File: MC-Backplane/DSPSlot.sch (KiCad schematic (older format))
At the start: 0 parts

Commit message: added reverse polarity protection circuit and fuse
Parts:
- added J?: DB37_Female, symbol Connector:DB37_Female
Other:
- note added: "placeholder connector"
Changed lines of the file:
@@
 $Descr A4 11693 8268
 encoding utf-8
-Sheet 1 5
+Sheet 5 5
 Title ""
 Date ""
@@
 Comment4 ""
 $EndDescr
+$Comp
+L Connector:DB37_Female J?
+U 1 1 61EE6699
+P 9050 3750
+F 0 "J?" H 9230 3784 50  0000 L CNN
+F 1 "DB37_Female" H 9230 3693 50  0000 L CNN
+F 2 "" H 9050 3750 50  0001 C CNN
+F 3 " ~" H 9050 3750 50  0001 C CNN
+	1    9050 3750
+	1    0    0    -1
+$EndComp
+Text Notes 9400 1550 0    50   ~ 0
+placeholder connector
 $EndSCHEMATC

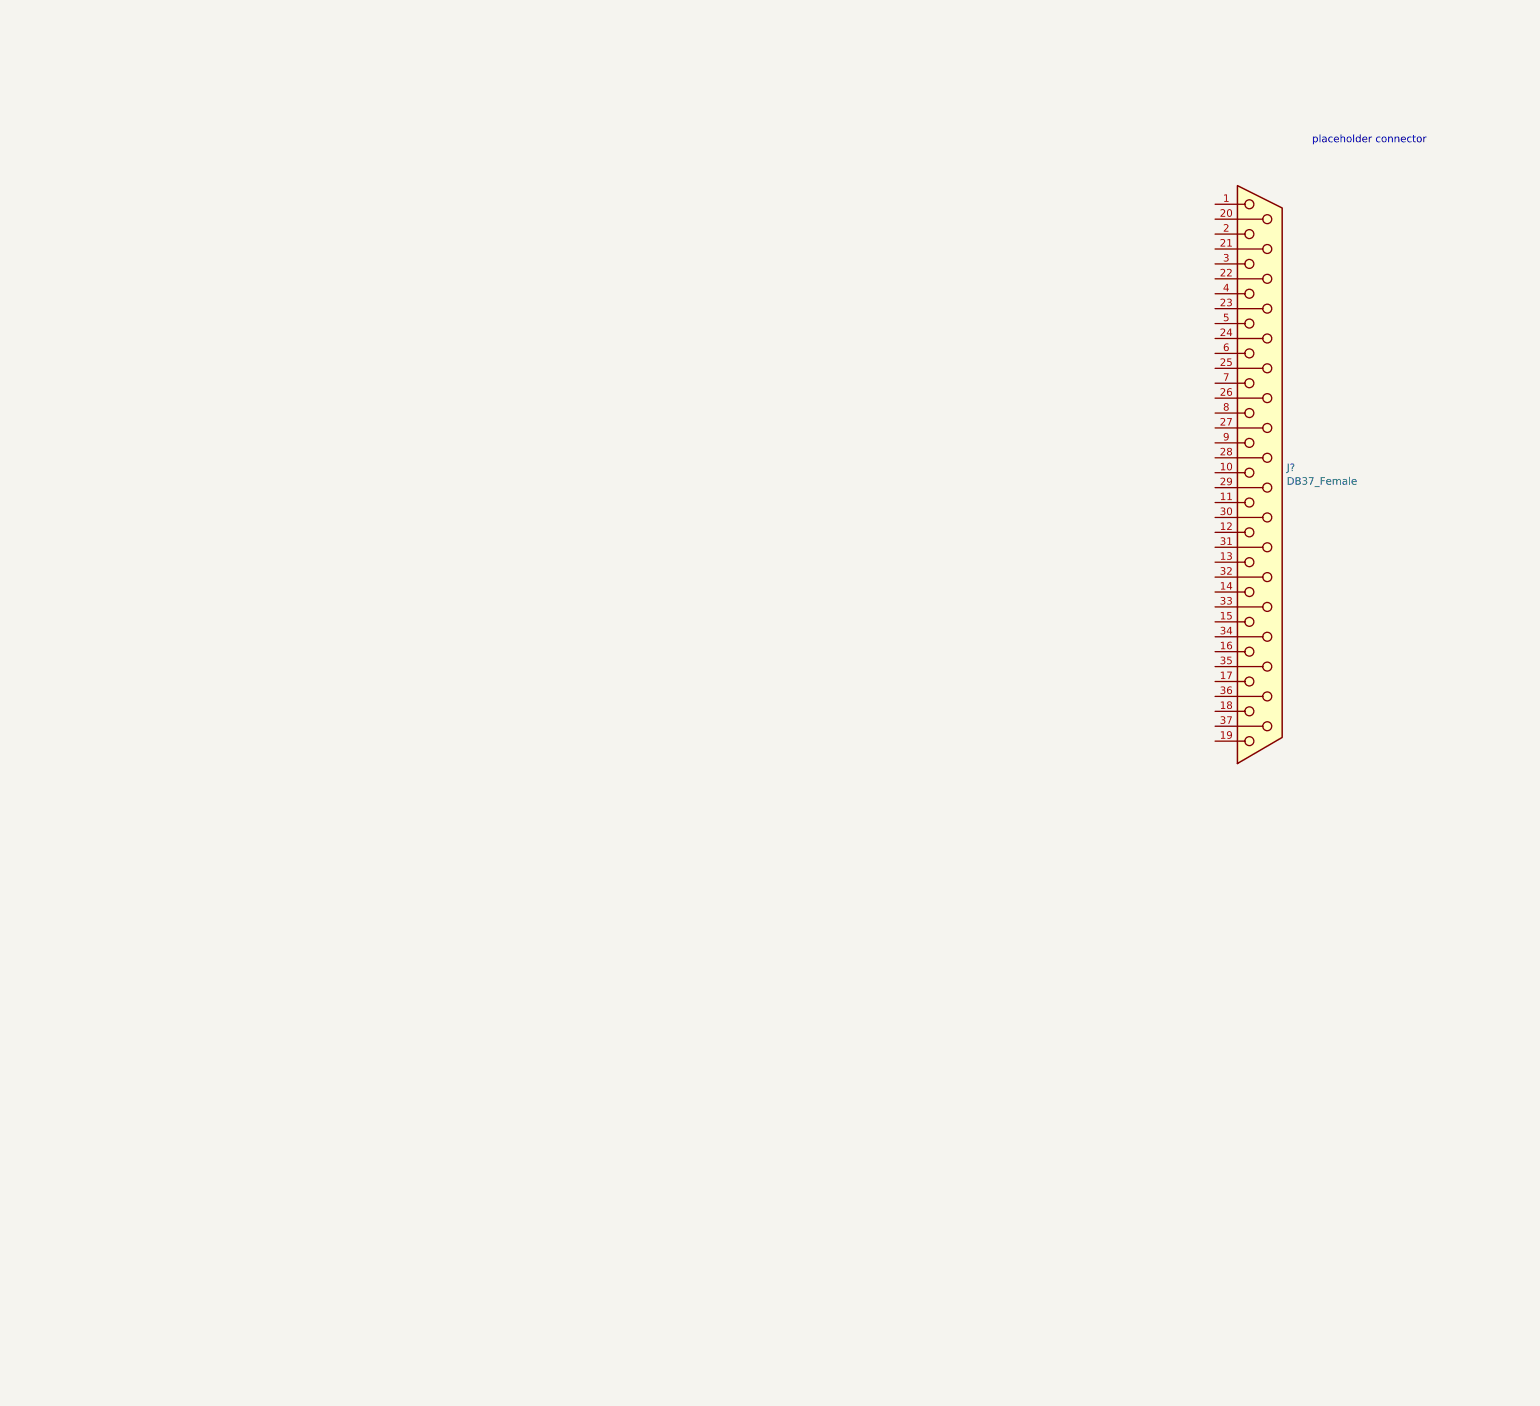
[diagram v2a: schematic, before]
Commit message: added signals for FO slots
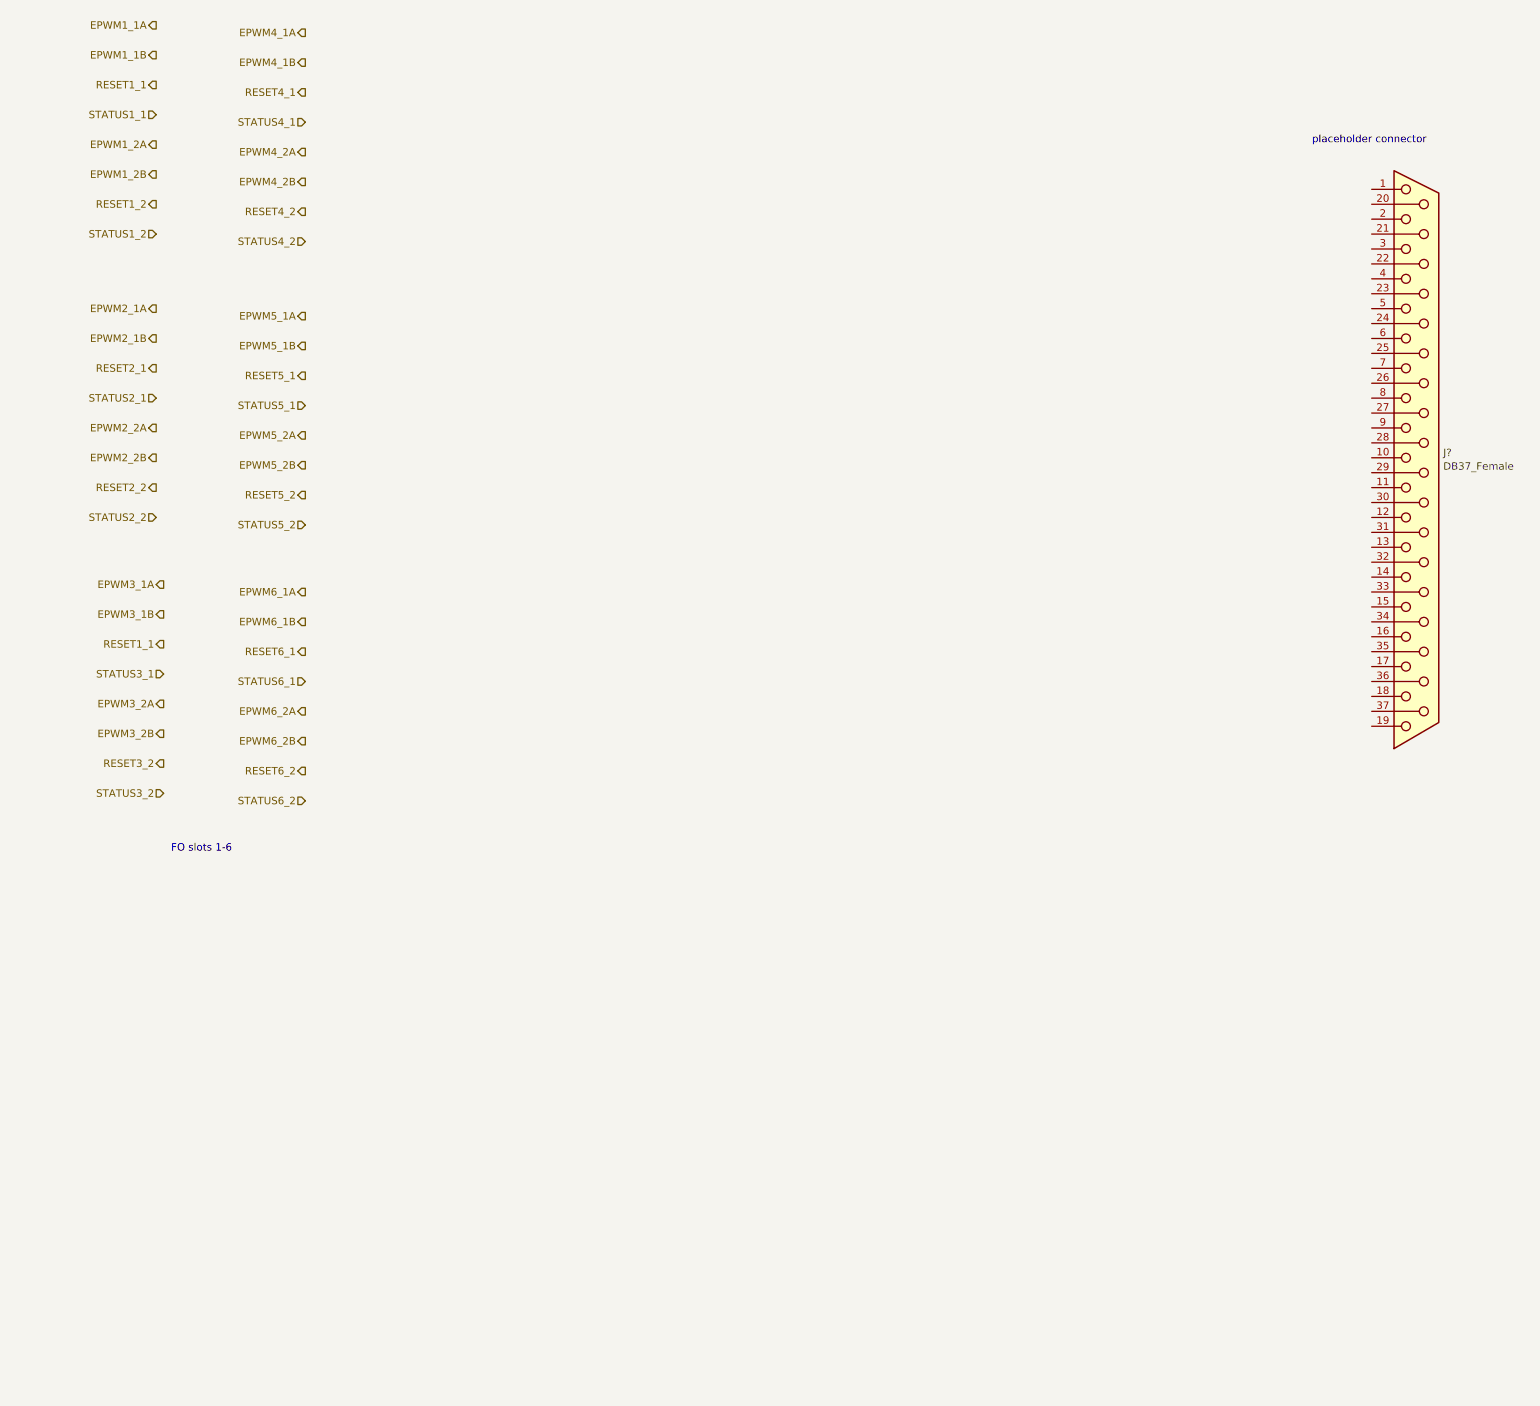
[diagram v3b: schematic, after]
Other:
- note added: "FO slots 1-6"
- moved on the sheet: J?
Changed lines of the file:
@@
 $Descr A4 11693 8268
 encoding utf-8
-Sheet 5 6
+Sheet 4 7
 Title ""
 Date ""
@@
 L Connector:DB37_Female J?
 U 1 1 61EE6699
-P 9050 3750
-F 0 "J?" H 9230 3784 50  0000 L CNN
-F 1 "DB37_Female" H 9230 3693 50  0000 L CNN
-F 2 "" H 9050 3750 50  0001 C CNN
-F 3 " ~" H 9050 3750 50  0001 C CNN
-	1    9050 3750
+P 10100 3650
+F 0 "J?" H 10280 3684 50  0000 L CNN
+F 1 "DB37_Female" H 10280 3593 50  0000 L CNN
+F 2 "" H 10100 3650 50  0001 C CNN
+F 3 " ~" H 10100 3650 50  0001 C CNN
+	1    10100 3650
 	1    0    0    -1
 $EndComp
 Text Notes 9400 1550 0    50   ~ 0
 placeholder connector
+Text HLabel 1650 750  0    50   Output ~ 0
+EPWM1_1A
+Text HLabel 1650 950  0    50   Output ~ 0
+EPWM1_1B
+Text HLabel 1650 1150 0    50   Output ~ 0
+RESET1_1
+Text HLabel 1650 1350 0    50   Input ~ 0
+STATUS1_1
+Text HLabel 1650 1550 0    50   Output ~ 0
+EPWM1_2A
+Text HLabel 1650 1750 0    50   Output ~ 0
+EPWM1_2B
+Text HLabel 1650 1950 0    50   Output ~ 0
+RESET1_2
+Text HLabel 1650 2150 0    50   Input ~ 0
+STATUS1_2
+Text HLabel 1650 2650 0    50   Output ~ 0
+EPWM2_1A
+Text HLabel 1650 2850 0    50   Output ~ 0
+EPWM2_1B
+Text HLabel 1650 3050 0    50   Output ~ 0
+RESET2_1
+Text HLabel 1650 3250 0    50   Input ~ 0
+STATUS2_1
+Text HLabel 1650 3450 0    50   Output ~ 0
+EPWM2_2A
+Text HLabel 1650 3650 0    50   Output ~ 0
+EPWM2_2B
+Text HLabel 1650 3850 0    50   Output ~ 0
+RESET2_2
+Text HLabel 1650 4050 0    50   Input ~ 0
+STATUS2_2
+Text HLabel 1700 4500 0    50   Output ~ 0
+EPWM3_1A
+Text HLabel 1700 4700 0    50   Output ~ 0
+EPWM3_1B
+Text HLabel 1700 4900 0    50   Output ~ 0
+RESET1_1
+Text HLabel 1700 5100 0    50   Input ~ 0
+STATUS3_1
+Text HLabel 1700 5300 0    50   Output ~ 0
+EPWM3_2A
+Text HLabel 1700 5500 0    50   Output ~ 0
+EPWM3_2B
+Text HLabel 1700 5700 0    50   Output ~ 0
+RESET3_2
+Text HLabel 1700 5900 0    50   Input ~ 0
+STATUS3_2
+Text HLabel 2650 800  0    50   Output ~ 0
+EPWM4_1A
+Text HLabel 2650 1000 0    50   Output ~ 0
+EPWM4_1B
+Text HLabel 2650 1200 0    50   Output ~ 0
+RESET4_1
+Text HLabel 2650 1400 0    50   Input ~ 0
+STATUS4_1
+Text HLabel 2650 1600 0    50   Output ~ 0
+EPWM4_2A
+Text HLabel 2650 1800 0    50   Output ~ 0
+EPWM4_2B
+Text HLabel 2650 2000 0    50   Output ~ 0
+RESET4_2
+Text HLabel 2650 2200 0    50   Input ~ 0
+STATUS4_2
+Text HLabel 2650 4100 0    50   Input ~ 0
+STATUS5_2
+Text HLabel 2650 3900 0    50   Output ~ 0
+RESET5_2
+Text HLabel 2650 3700 0    50   Output ~ 0
+EPWM5_2B
+Text HLabel 2650 3500 0    50   Output ~ 0
+EPWM5_2A
+Text HLabel 2650 3300 0    50   Input ~ 0
+STATUS5_1
+Text HLabel 2650 3100 0    50   Output ~ 0
+RESET5_1
+Text HLabel 2650 2900 0    50   Output ~ 0
+EPWM5_1B
+Text HLabel 2650 2700 0    50   Output ~ 0
+EPWM5_1A
+Text HLabel 2650 5950 0    50   Input ~ 0
+STATUS6_2
+Text HLabel 2650 5750 0    50   Output ~ 0
+RESET6_2
+Text HLabel 2650 5550 0    50   Output ~ 0
+EPWM6_2B
+Text HLabel 2650 5350 0    50   Output ~ 0
+EPWM6_2A
+Text HLabel 2650 5150 0    50   Input ~ 0
+STATUS6_1
+Text HLabel 2650 4950 0    50   Output ~ 0
+RESET6_1
+Text HLabel 2650 4750 0    50   Output ~ 0
+EPWM6_1B
+Text HLabel 2650 4550 0    50   Output ~ 0
+EPWM6_1A
+Text Notes 1750 6300 0    50   ~ 0
+FO slots 1-6
 $EndSCHEMATC

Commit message: Add files via upload
updating net names and wires
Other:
- note added: "Analog slots"
- note added: "Delta Sigma Slots"
- note added: "Get final connector and pinout from jacob"
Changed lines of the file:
@@
 $Descr A4 11693 8268
 encoding utf-8
-Sheet 4 7
+Sheet 3 7
 Title ""
 Date ""
@@
 placeholder connector
 Text HLabel 1650 750  0    50   Output ~ 0
-EPWM1_1A
+GD_EPWM1_1A
 Text HLabel 1650 950  0    50   Output ~ 0
-EPWM1_1B
+GD_EPWM1_1B
 Text HLabel 1650 1150 0    50   Output ~ 0
-RESET1_1
+GD_RESET1_1
 Text HLabel 1650 1350 0    50   Input ~ 0
-STATUS1_1
+GD_DPWM_STATUS1_1
 Text HLabel 1650 1550 0    50   Output ~ 0
-EPWM1_2A
+GD_EPWM1_2A
 Text HLabel 1650 1750 0    50   Output ~ 0
-EPWM1_2B
+GD_EPWM1_2B
 Text HLabel 1650 1950 0    50   Output ~ 0
-RESET1_2
+GD_RESET1_2
 Text HLabel 1650 2150 0    50   Input ~ 0
-STATUS1_2
+GD_DPWM_STATUS1_2
 Text HLabel 1650 2650 0    50   Output ~ 0
-EPWM2_1A
+GD_EPWM2_1A
 Text HLabel 1650 2850 0    50   Output ~ 0
-EPWM2_1B
+GD_EPWM2_1B
 Text HLabel 1650 3050 0    50   Output ~ 0
-RESET2_1
+GD_RESET2_1
 Text HLabel 1650 3250 0    50   Input ~ 0
-STATUS2_1
+GD_DPWM_STATUS2_1
 Text HLabel 1650 3450 0    50   Output ~ 0
-EPWM2_2A
+GD_EPWM2_2A
 Text HLabel 1650 3650 0    50   Output ~ 0
-EPWM2_2B
+GD_EPWM2_2B
 Text HLabel 1650 3850 0    50   Output ~ 0
-RESET2_2
+GD_RESET2_2
 Text HLabel 1650 4050 0    50   Input ~ 0
-STATUS2_2
+GD_DPWM_STATUS2_2
 Text HLabel 1700 4500 0    50   Output ~ 0
-EPWM3_1A
+GD_EPWM3_1A
 Text HLabel 1700 4700 0    50   Output ~ 0
-EPWM3_1B
+GD_EPWM3_1B
 Text HLabel 1700 4900 0    50   Output ~ 0
-RESET1_1
+GD_RESET1_1
 Text HLabel 1700 5100 0    50   Input ~ 0
-STATUS3_1
+GD_DPWM_STATUS3_1
 Text HLabel 1700 5300 0    50   Output ~ 0
-EPWM3_2A
+GD_EPWM3_2A
 Text HLabel 1700 5500 0    50   Output ~ 0
-EPWM3_2B
+GD_EPWM3_2B
 Text HLabel 1700 5700 0    50   Output ~ 0
-RESET3_2
+GD_RESET3_2
 Text HLabel 1700 5900 0    50   Input ~ 0
-STATUS3_2
+GD_DPWM_STATUS3_2
 Text HLabel 2650 800  0    50   Output ~ 0
-EPWM4_1A
+GD_EPWM4_1A
 Text HLabel 2650 1000 0    50   Output ~ 0
-EPWM4_1B
+GD_EPWM4_1B
 Text HLabel 2650 1200 0    50   Output ~ 0
-RESET4_1
+GD_RESET4_1
 Text HLabel 2650 1400 0    50   Input ~ 0
-STATUS4_1
+GD_DPWM_STATUS4_1
 Text HLabel 2650 1600 0    50   Output ~ 0
-EPWM4_2A
+GD_EPWM4_2A
 Text HLabel 2650 1800 0    50   Output ~ 0
-EPWM4_2B
+GD_EPWM4_2B
 Text HLabel 2650 2000 0    50   Output ~ 0
-RESET4_2
+GD_RESET4_2
 Text HLabel 2650 2200 0    50   Input ~ 0
-STATUS4_2
+GD_DPWM_STATUS4_2
 Text HLabel 2650 4100 0    50   Input ~ 0
-STATUS5_2
+GD_DPWM_STATUS5_2
 Text HLabel 2650 3900 0    50   Output ~ 0
-RESET5_2
+GD_RESET5_2
 Text HLabel 2650 3700 0    50   Output ~ 0
-EPWM5_2B
+GD_EPWM5_2B
 Text HLabel 2650 3500 0    50   Output ~ 0
-EPWM5_2A
+GD_EPWM5_2A
 Text HLabel 2650 3300 0    50   Input ~ 0
-STATUS5_1
+GD_DPWM_STATUS5_1
 Text HLabel 2650 3100 0    50   Output ~ 0
-RESET5_1
+GD_RESET5_1
 Text HLabel 2650 2900 0    50   Output ~ 0
-EPWM5_1B
+GD_EPWM5_1B
 Text HLabel 2650 2700 0    50   Output ~ 0
-EPWM5_1A
+GD_EPWM5_1A
 Text HLabel 2650 5950 0    50   Input ~ 0
-STATUS6_2
+GD_DPWM_STATUS6_2
 Text HLabel 2650 5750 0    50   Output ~ 0
-RESET6_2
+GD_RESET6_2
 Text HLabel 2650 5550 0    50   Output ~ 0
-EPWM6_2B
+GD_EPWM6_2B
 Text HLabel 2650 5350 0    50   Output ~ 0
-EPWM6_2A
+GD_EPWM6_2A
 Text HLabel 2650 5150 0    50   Input ~ 0
-STATUS6_1
+GD_DPWM_STATUS6_1
 Text HLabel 2650 4950 0    50   Output ~ 0
-RESET6_1
+GD_RESET6_1
 Text HLabel 2650 4750 0    50   Output ~ 0
-EPWM6_1B
+GD_EPWM6_1B
 Text HLabel 2650 4550 0    50   Output ~ 0
-EPWM6_1A
+GD_EPWM6_1A
 Text Notes 1750 6300 0    50   ~ 0
 FO slots 1-6
+Text HLabel 8850 1450 0    50   Output ~ 0
+CLOCK
+Text HLabel 9000 2650 0    50   Output ~ 0
+EMITTER_ENABLE
+Text HLabel 9050 2500 0    50   BiDi ~ 0
+SAFE_STATE_FLAG
+Text HLabel 8850 1600 0    50   Output ~ 0
+GND
+Text HLabel 8800 1350 0    50   Input ~ 0
+24V
+Text HLabel 5500 1500 0    50   Output ~ 0
+ADCINA2
+Text HLabel 5500 1700 0    50   Output ~ 0
+ADCINA3
+Text HLabel 5500 1900 0    50   Output ~ 0
+ADCINA4
+Text HLabel 5500 2100 0    50   Output ~ 0
+ADCINA5
+Text HLabel 5500 2300 0    50   Output ~ 0
+ADCIN14
+Text HLabel 5500 2500 0    50   Output ~ 0
+ADCIN15
+Text HLabel 6550 1500 0    50   Output ~ 0
+ADCINB2
+Text HLabel 6550 1700 0    50   Output ~ 0
+ADCINB3
+Text HLabel 6550 1900 0    50   Output ~ 0
+ADCINC2
+Text HLabel 6550 2100 0    50   Output ~ 0
+ADCINC3
+Text HLabel 6550 2300 0    50   Output ~ 0
+ADCINC4
+Text HLabel 6550 2500 0    50   Output ~ 0
+ADCINC5
+Text HLabel 5800 5950 0    50   Output ~ 0
+DS_Epwm_A1
+Text HLabel 5800 6150 0    50   Output ~ 0
+DS_Epwm_A2
+Text HLabel 5800 6350 0    50   Output ~ 0
+DS_Epwm_A3
+Text HLabel 5800 6550 0    50   Output ~ 0
+DS_Epwm_A4
+Text HLabel 5700 5600 0    50   Output ~ 0
+DS_SD_A
+Text HLabel 5700 5750 0    50   Output ~ 0
+DS_Clk_A
+Text HLabel 5800 4550 0    50   Input ~ 0
+DS_GPIO_D_A1
+Text HLabel 5800 4750 0    50   Input ~ 0
+DS_GPIO_D_A2
+Text HLabel 5800 4950 0    50   Input ~ 0
+DS_GPIO_D_A3
+Text HLabel 5800 5150 0    50   Input ~ 0
+DS_GPIO_D_A4
+Text HLabel 7000 5850 0    50   Output ~ 0
+DS_Epwm_B1
+Text HLabel 7000 6000 0    50   Output ~ 0
+DS_Epwm_B2
+Text HLabel 7000 6150 0    50   Output ~ 0
+DS_Epwm_B3
+Text HLabel 7000 6300 0    50   Output ~ 0
+DS_Epwm_B4
+Text HLabel 6950 5500 0    50   Output ~ 0
+DS_SD_B
+Text HLabel 6950 5650 0    50   Output ~ 0
+DS_Clk_B
+Text HLabel 7050 4700 0    50   Input ~ 0
+DS_GPIO_D_B1
+Text HLabel 7050 4800 0    50   Input ~ 0
+DS_GPIO_D_B2
+Text HLabel 7050 4900 0    50   Input ~ 0
+DS_GPIO_D_B3
+Text HLabel 7050 5000 0    50   Input ~ 0
+DS_GPIO_D_B4
+Text Notes 5600 1050 0    50   ~ 0
+Analog slots
+Text Notes 5800 4400 0    50   ~ 0
+Delta Sigma Slots
+Text Notes 8750 900  0    50   ~ 0
+Get final connector and pinout from jacob
 $EndSCHEMATC
